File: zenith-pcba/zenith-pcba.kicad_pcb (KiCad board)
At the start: 2 copper layers, 11 parts, among them SW1 G4R152312, U1 XC7A50T-CSG325, U2 K4B4G1646E-BCNB, U3 CH347T, X1 SX5B8.000F1520F30

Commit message: fix(pcba): data routing
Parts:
- moved R2 140.4 mm to (69.5, 44.6)
- moved C2 136.7 mm to (77.2, 54.0), turned to 180 degrees
- moved R1 136.5 mm to (72.8, 44.6)
- moved C3 131.0 mm to (83.6, 49.4), turned to -90 degrees
- moved SW1 129.5 mm to (80.0, 45.0)
- moved C1 129.4 mm to (85.2, 48.8), turned to 90 degrees
- moved X1 129.1 mm to (79.8, 50.8)
- moved U3 110.4 mm to (71.2, 49.0), turned to 90 degrees
- moved USB1 91.3 mm to (61.6, 49.3), turned to -90 degrees
- moved U1 89.7 mm to (77.2, 109.6)
- moved U2 55.8 mm to (105.0, 105.4)
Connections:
- SW1 pad 5: unconnected-(SW1-NC-Pad5) -> GND
- SW1 pad 6: unconnected-(SW1-NC-Pad6) -> GND
- USB1 pad A1: unconnected-(USB1-GND-PadA1) -> GND
- USB1 pad A12: unconnected-(USB1-GND-PadA12) -> GND
- USB1 pad A6: unconnected-(USB1-DP1-PadA6) -> Net-(U3-UD+)
- USB1 pad A7: unconnected-(USB1-DN1-PadA7) -> Net-(U3-UD-)
- USB1 pad B1: unconnected-(USB1-GND-PadB1) -> GND
- USB1 pad B12: unconnected-(USB1-GND-PadB12) -> GND
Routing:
- net GND: track 0.00 -> 24.1 mm, vias 0 -> 15
- net Net-(U3-XI): track 0.00 -> 17.3 mm
- net Net-(U3-~{RST}): track 0.00 -> 13.8 mm
- net Net-(U3-XO): track 0.00 -> 12.1 mm
- net Net-(U3-UD+): track 0.00 -> 7.08 mm
- net Net-(U3-UD-): track 0.00 -> 6.25 mm
- net Net-(U3-RTS1/GPIO7): track 0.00 -> 4.81 mm
- net Net-(U3-TNOW1/DTR1): track 0.00 -> 1.71 mm
- added copper zone on B.Cu, net GND
- removed copper zone on B.Cu, net (none)
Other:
- board text added: "RESET"

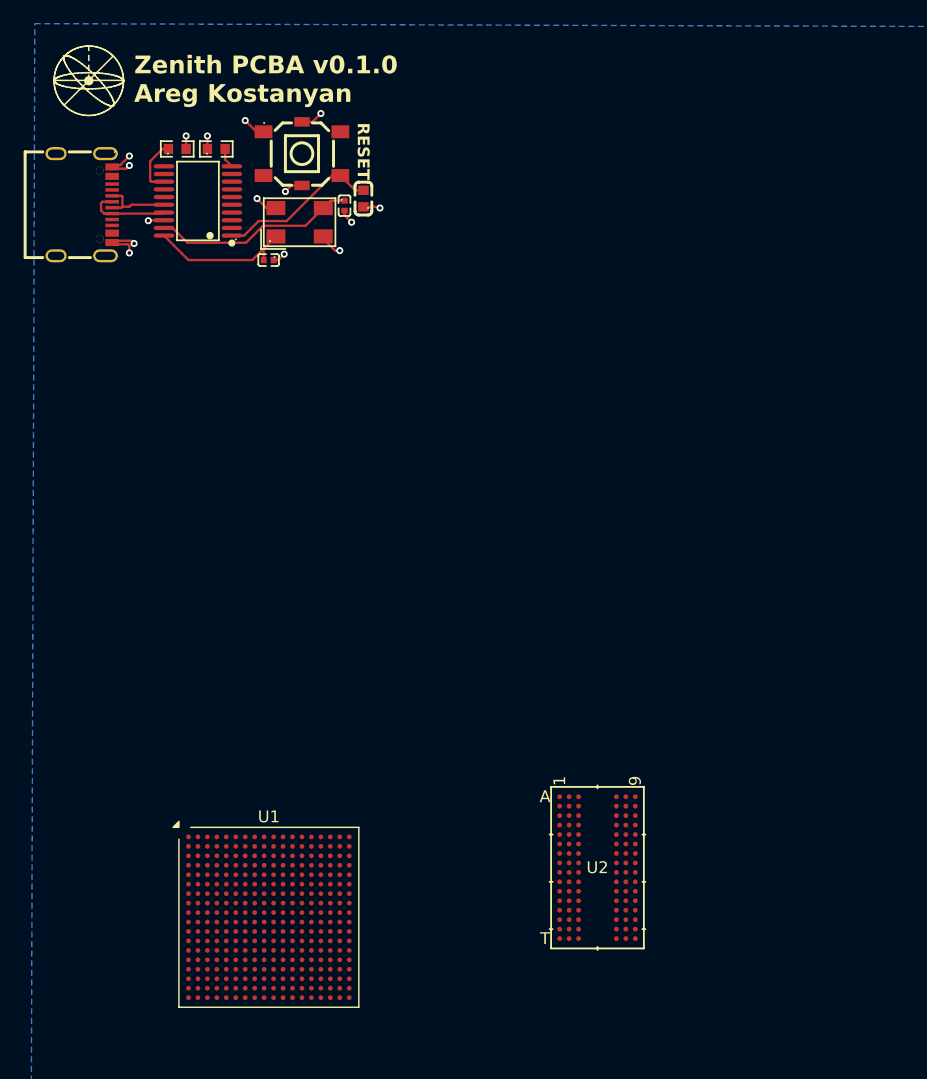
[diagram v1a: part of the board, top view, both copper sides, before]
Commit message: feat(pcba): usb esd
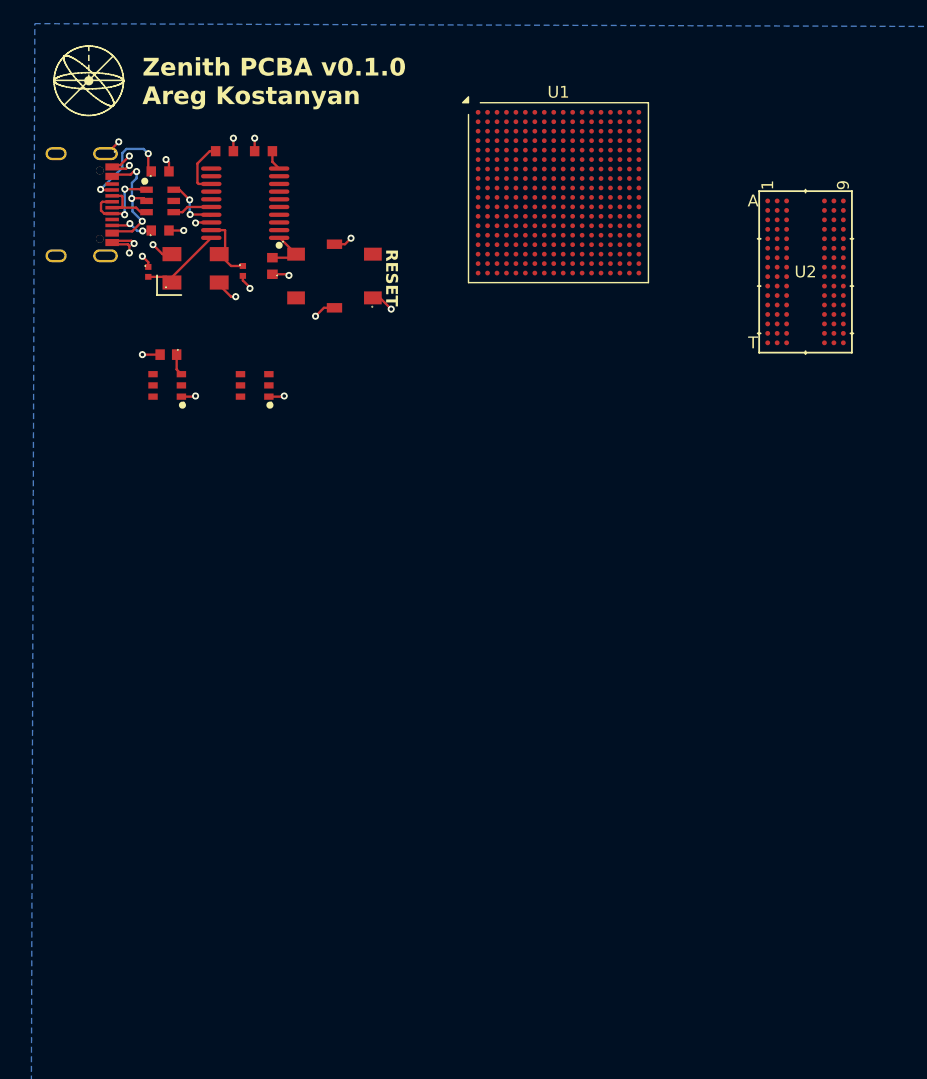
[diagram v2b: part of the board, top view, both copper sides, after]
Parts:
- added C4: CC0603MRX5R7BB106, easyeda2kicad:C0603, F.Cu at (68.7, 62.0)
- added D1: USBLC6-2SC6, easyeda2kicad:SOT-23-6_L2.9-W1.6-P0.95-LS2.8-BL, F.Cu at (68.0, 49.0)
- added R3: RC0603JR-075K1L, easyeda2kicad:R0603, F.Cu at (68.0, 46.5)
- added R4: RC0603JR-075K1L, easyeda2kicad:R0603, F.Cu at (68.0, 51.5)
- added U4: TPS54302DDCT, easyeda2kicad:TSOT-23-6_L2.9-W1.6-P0.95-LS2.8-BR, F.Cu at (68.6, 64.6)
- added U5: TPS54302DDCT, easyeda2kicad:TSOT-23-6_L2.9-W1.6-P0.95-LS2.8-BR, F.Cu at (76.0, 64.6)
- moved U1 66.0 mm to (101.7, 48.3)
- moved U2 53.4 mm to (122.6, 55.0)
- moved SW1 10.7 mm to (82.8, 55.4), turned to 180 degrees
- moved C2 10.2 mm to (67.0, 55.0), turned to -90 degrees
- moved C3 10.2 mm to (75.0, 54.9)
- moved X1 9.63 mm to (71.0, 54.7)
- moved C1 9.58 mm to (77.5, 54.5)
- moved R1 4.00 mm to (76.8, 44.8)
- moved R2 4.00 mm to (73.5, 44.8)
- moved U3 4.00 mm to (75.2, 49.2)
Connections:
- U3 pad 16: Net-(U3-UD-) -> /Programmer/D-out
- U3 pad 17: Net-(U3-UD+) -> /Programmer/D+out
- USB1 pad 1: unconnected-(USB1-EH-Pad1) -> GND
- USB1 pad A4: unconnected-(USB1-VBUS-PadA4) -> /Programmer/VBUSin
- USB1 pad A5: unconnected-(USB1-CC1-PadA5) -> Net-(USB1-CC1)
- USB1 pad A6: Net-(U3-UD+) -> /Programmer/D+in
- USB1 pad A7: Net-(U3-UD-) -> /Programmer/D-in
- USB1 pad A9: unconnected-(USB1-VBUS-PadA9) -> /Programmer/VBUSin
- USB1 pad B4: unconnected-(USB1-VBUS-PadB4) -> /Programmer/VBUSin
- USB1 pad B5: unconnected-(USB1-CC2-PadB5) -> Net-(USB1-CC2)
- USB1 pad B6: Net-(U3-UD+) -> /Programmer/D+in
- USB1 pad B7: Net-(U3-UD-) -> /Programmer/D-in
- USB1 pad B9: unconnected-(USB1-VBUS-PadB9) -> /Programmer/VBUSin
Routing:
- net Net-(U3-XI): track 17.3 -> 5.80 mm
- net /Programmer/VBUSin: track 0.00 -> 11.3 mm, vias 0 -> 3
- net Net-(U3-~{RST}): track 13.8 -> 4.13 mm
- net Net-(USB1-CC1): track 0.00 -> 8.94 mm, vias 0 -> 2
- net GND: track 24.1 -> 31.9 mm, vias 15 -> 21
- net /Programmer/D+in: track 0.00 -> 7.28 mm, vias 0 -> 2
- net Net-(U3-UD+): track 7.08 -> 0.00 mm
- net Net-(U3-UD-): track 6.25 -> 0.00 mm
- net /Programmer/D-in: track 0.00 -> 5.24 mm
- net /Programmer/D+out: track 0.00 -> 4.89 mm, vias 0 -> 2
- net Net-(U3-XO): track 12.1 -> 7.36 mm
- net Net-(USB1-CC2): track 0.00 -> 3.65 mm, vias 0 -> 2
- net /Programmer/D-out: track 0.00 -> 3.36 mm
- net /Programmer/VBUSout: track 0.00 -> 1.82 mm

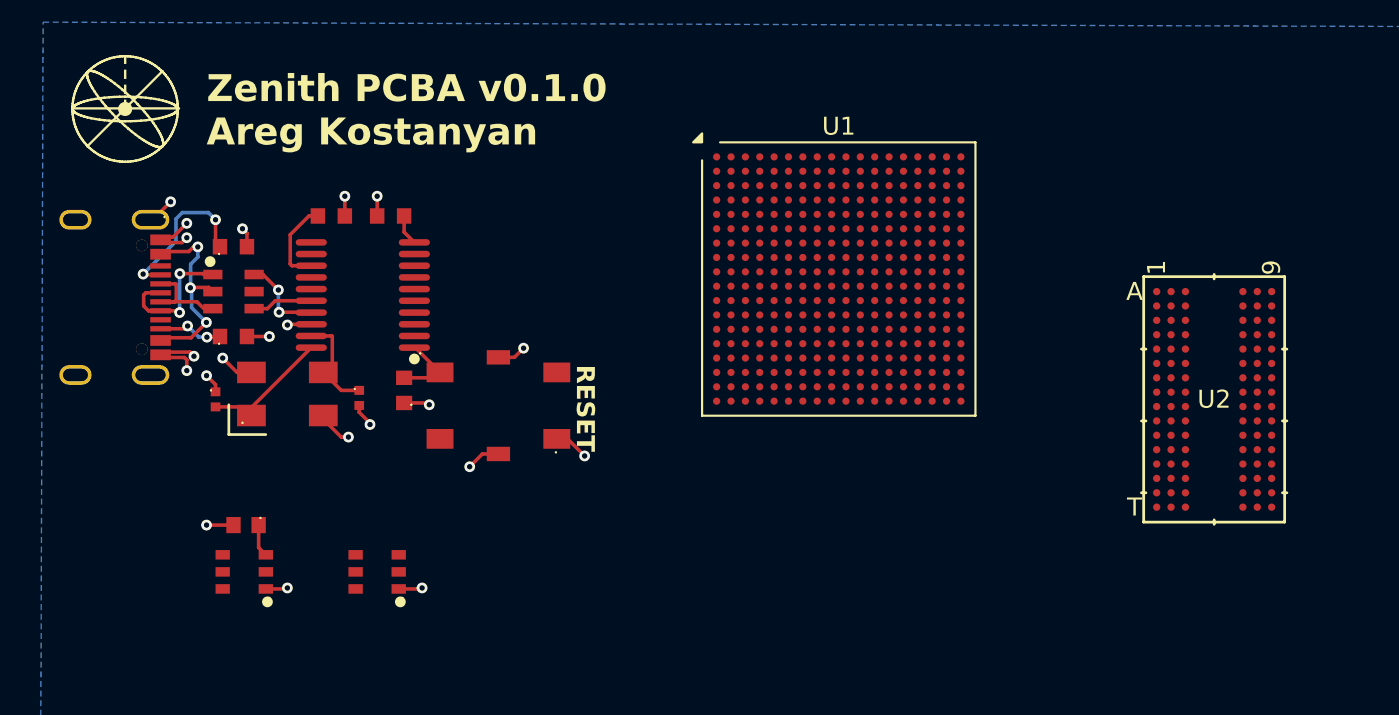
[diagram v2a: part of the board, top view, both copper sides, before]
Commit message: fix(pcba): usb c esd ground
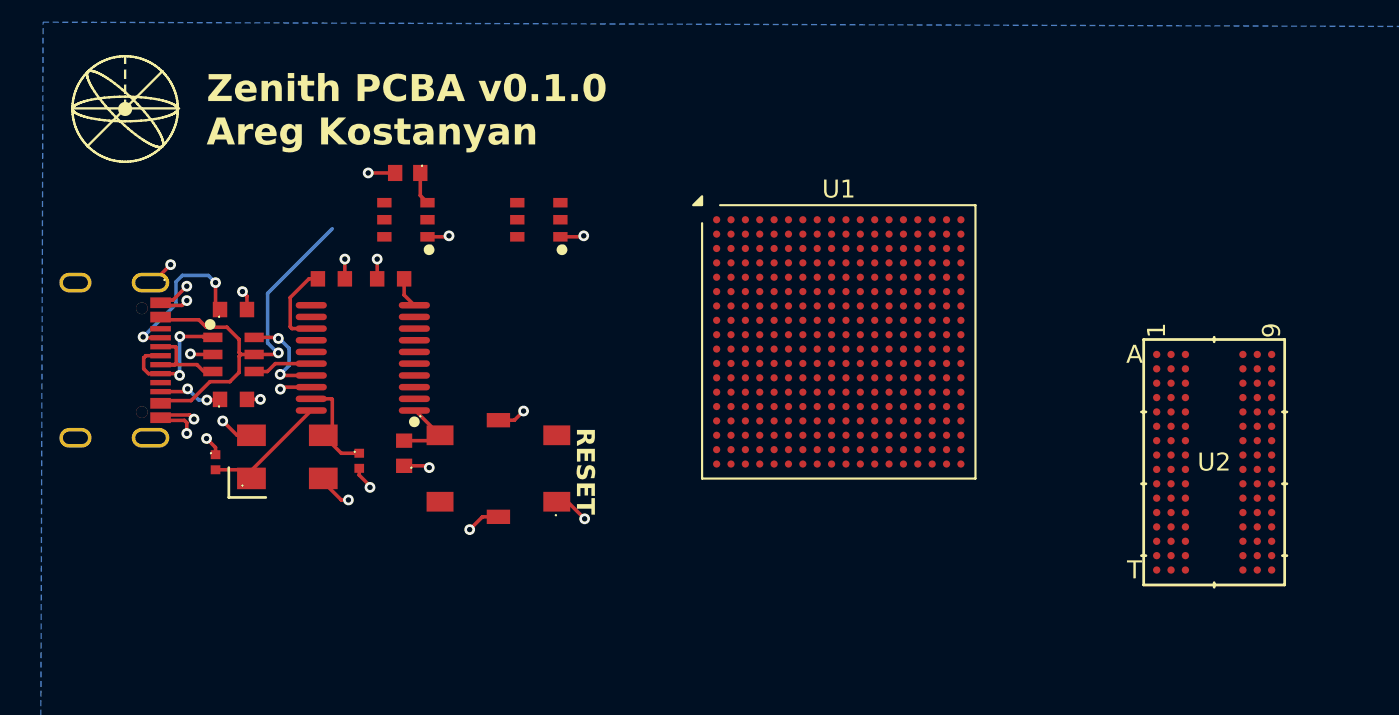
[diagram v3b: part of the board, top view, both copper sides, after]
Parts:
- moved U4 21.6 mm to (77.6, 45.0)
- moved U5 21.6 mm to (85.0, 45.0)
- moved C4 21.6 mm to (77.7, 42.4)
- moved C1 3.50 mm to (77.5, 58.0)
- moved C2 3.50 mm to (67.0, 58.5)
- moved C3 3.50 mm to (75.0, 58.4)
- moved D1 3.50 mm to (68.0, 52.5)
- moved R1 3.50 mm to (76.8, 48.3)
- moved R2 3.50 mm to (73.5, 48.3)
- moved R3 3.50 mm to (68.0, 50.0)
- moved R4 3.50 mm to (68.0, 55.0)
- moved SW1 3.50 mm to (82.8, 58.9)
- moved U1 3.50 mm to (101.7, 51.8)
- moved U2 3.50 mm to (122.6, 58.5)
- moved U3 3.50 mm to (75.2, 52.7)
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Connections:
- C4 pad 1: /Programmer/VBUSout -> /Programmer/VBUSin
- D1 pad 2: /Programmer/VBUSin -> GND
- D1 pad 5: /Programmer/VBUSout -> /Programmer/VBUSin
- U4 pad 3: /Programmer/VBUSout -> /Programmer/VBUSin
- U5 pad 3: /Programmer/VBUSout -> /Programmer/VBUSin
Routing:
- net /Programmer/VBUSin: track 11.3 -> 24.8 mm, vias 3 -> 1
- net /Programmer/VBUSout: track 1.82 -> 0.00 mm
- net GND: track 31.9 -> 33.2 mm, vias 21 -> 22
- net /Programmer/D+out: track 4.89 -> 5.76 mm

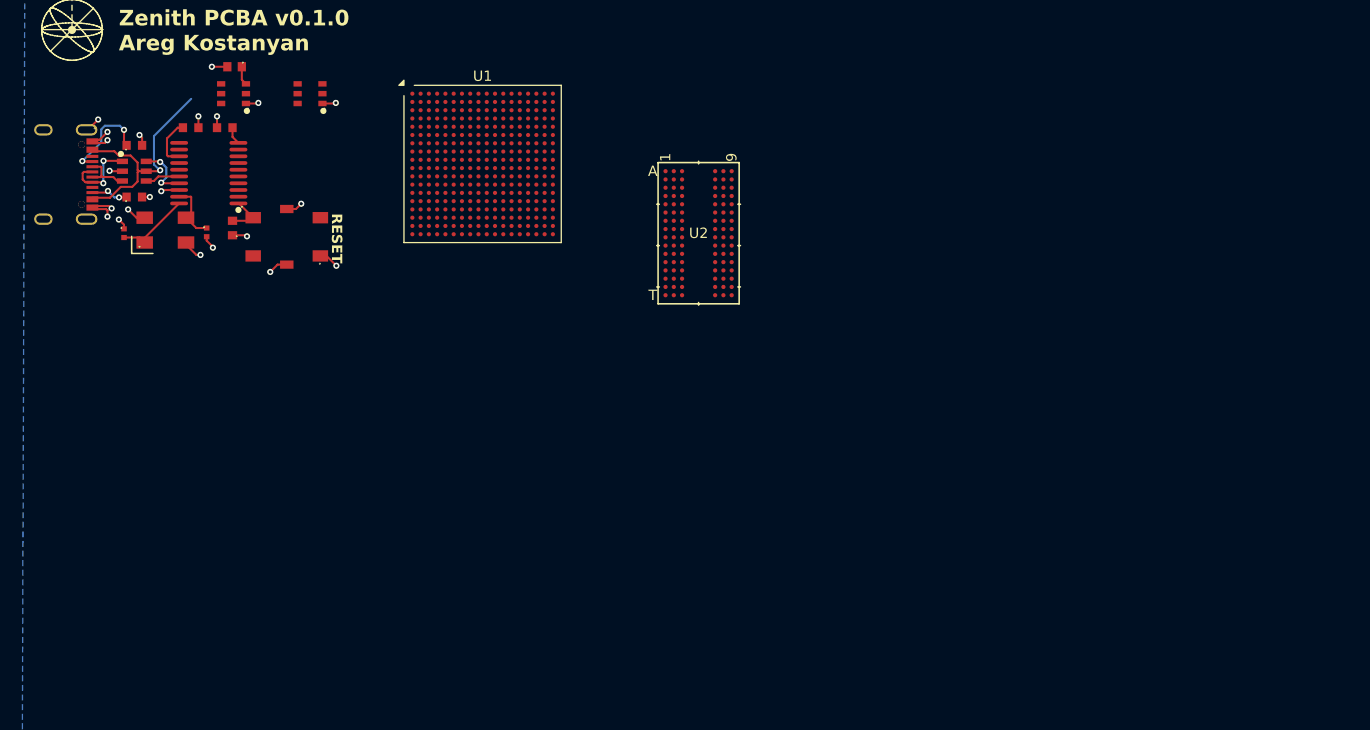
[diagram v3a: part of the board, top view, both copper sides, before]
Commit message: feat(pcba): 3.3v buck
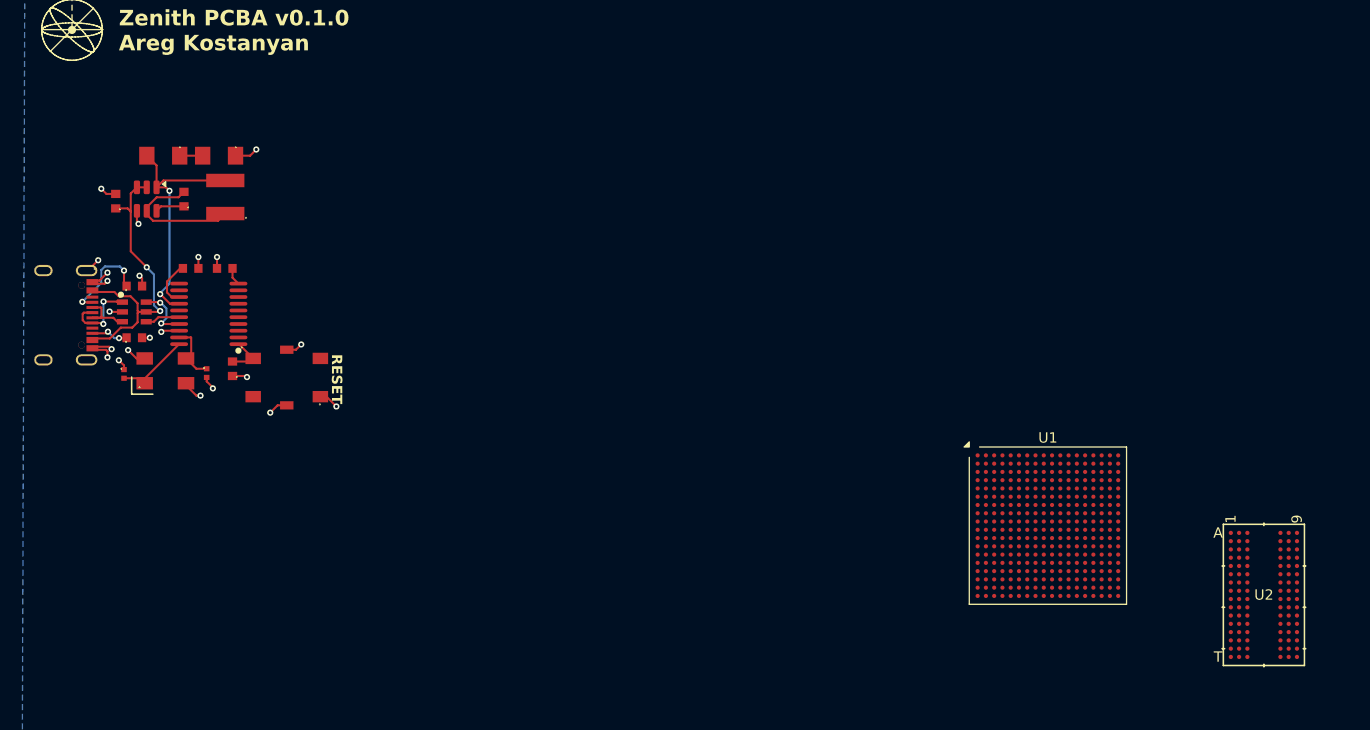
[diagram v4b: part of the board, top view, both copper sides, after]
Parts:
- removed U5: TPS54302DDCT, easyeda2kicad:TSOT-23-6_L2.9-W1.6-P0.95-LS2.8-BR
- added C5: CL10B104KA8NNNC, easyeda2kicad:C0603, F.Cu at (72.8, 55.2)
- added C6: CC1206KKX7R6BB226, easyeda2kicad:C1206, F.Cu at (70.8, 51.0)
- added C7: CC1206KKX7R6BB226, easyeda2kicad:C1206, F.Cu at (76.2, 51.0)
- added L2: SWPA4030S3R3MT, easyeda2kicad:IND-SMD_L4.0-W4.0_SMNR4012, F.Cu at (76.8, 55.0)
- U4: value TPS54302DDCT -> AP63203WU; footprint easyeda2kicad:TSOT-23-6_L2.9-W1.6-P0.95-LS2.8-BR -> Package_TO_SOT_SMD:TSOT-23-6
- moved U1 64.9 mm to (156.4, 86.8)
- moved U2 64.9 mm to (177.3, 93.5)
- moved C4 17.4 mm to (66.2, 55.4), turned to 90 degrees
- moved C1 13.6 mm to (77.5, 71.6)
- moved C2 13.6 mm to (67.0, 72.1)
- moved D1 13.6 mm to (68.0, 66.1)
- moved R4 13.6 mm to (68.0, 68.6)
- moved U3 13.6 mm to (75.2, 66.3)
- moved R1 13.6 mm to (76.8, 61.9)
- moved R2 13.6 mm to (73.5, 61.9)
- moved R3 13.6 mm to (68.0, 63.6)
- moved SW1 13.6 mm to (82.8, 72.5)
- moved USB1 13.6 mm to (61.6, 66.4)
- moved C3 13.6 mm to (75.0, 72.0)
- moved X1 13.6 mm to (71.0, 71.8)
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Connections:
- U3 pad 14: unconnected-(U3-VCC-Pad14) -> VCC3.3
- U4 pad 1: GND -> VCC3.3
- U4 pad 2: unconnected-(U4-SW-Pad2) -> /Programmer/VBUSin
- U4 pad 4: unconnected-(U4-FB-Pad4) -> GND
- U4 pad 5: unconnected-(U4-EN-Pad5) -> Net-(U4-SW)
- U4 pad 6: unconnected-(U4-BOOT-Pad6) -> Net-(U4-BST)
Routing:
- net VCC3.3: track 0.00 -> 24.4 mm, vias 0 -> 2
- net Net-(U4-SW): track 0.00 -> 13.1 mm
- net /Programmer/VBUSin: track 24.8 -> 30.3 mm, vias 1 -> 2
- net Net-(U4-BST): track 0.00 -> 2.83 mm
- net Net-(C6-Pad1): track 0.00 -> 2.22 mm
- net GND: track 33.2 -> 34.3 mm

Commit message: chore(pcba): labels
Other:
- board text added: "3.3"
- board text added: "ESD"
- board text added: "PROG"
